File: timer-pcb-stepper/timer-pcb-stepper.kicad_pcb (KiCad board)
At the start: 4 copper layers, 75 x 69.5 mm, 27 parts, among them J1 JST_05, J10 JST_05, J2 JST_02, J3 JST_02, J4 JST_03, J5 JST_03, J6 JST_03, J7 JST_03, J8 JST_03_Led_panel, J9 JST_05, U2 ULN2003, U3 ULN2003, U4 ULN2003

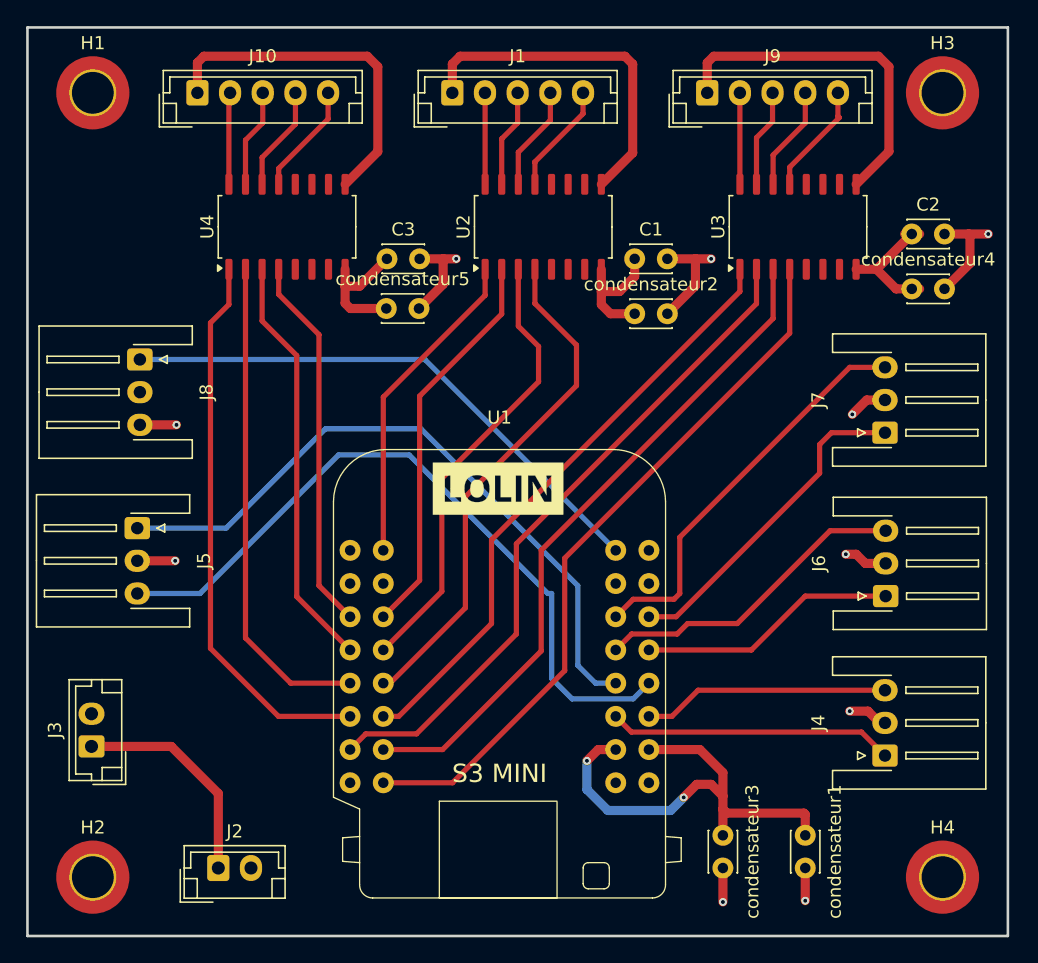
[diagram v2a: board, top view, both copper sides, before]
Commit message: rework des PCB stepper et led. création du PCB chargeur
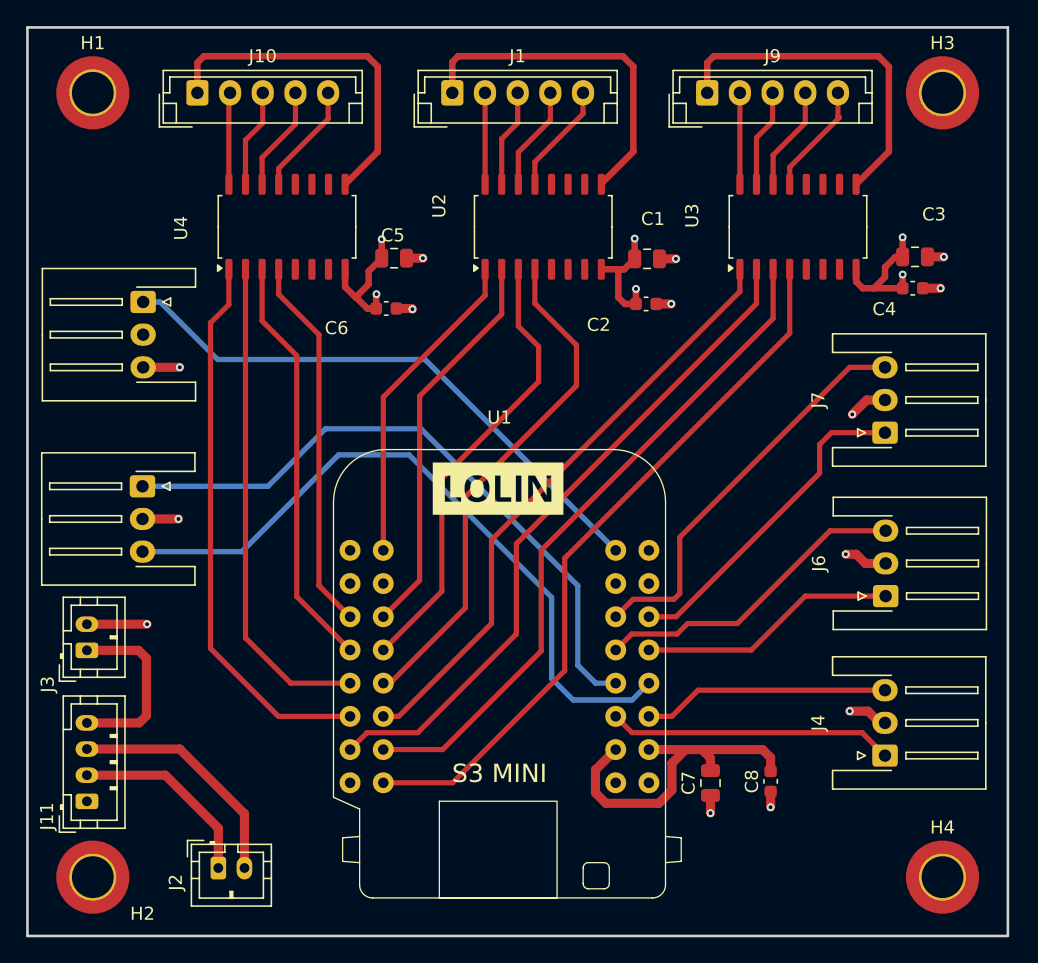
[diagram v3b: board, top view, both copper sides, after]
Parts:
- added J11: JST_04, Connector_JST:JST_PH_B4B-PH-K_1x04_P2.00mm_Vertical, F.Cu at (54.5, 99.2)
- C1: footprint Capacitor_THT:C_Disc_D3.0mm_W2.0mm_P2.50mm -> Capacitor_SMD:C_0805_2012Metric
- C2: renamed from condensateur2; footprint Capacitor_THT:C_Disc_D3.0mm_W2.0mm_P2.50mm -> Capacitor_SMD:C_0603_1608Metric
- C3: renamed from C2; footprint Capacitor_THT:C_Disc_D3.0mm_W2.0mm_P2.50mm -> Capacitor_SMD:C_0805_2012Metric
- C4: renamed from condensateur4; footprint Capacitor_THT:C_Disc_D3.0mm_W2.0mm_P2.50mm -> Capacitor_SMD:C_0603_1608Metric
- C5: renamed from C3; footprint Capacitor_THT:C_Disc_D3.0mm_W2.0mm_P2.50mm -> Capacitor_SMD:C_0805_2012Metric
- C6: renamed from condensateur5; footprint Capacitor_THT:C_Disc_D3.0mm_W2.0mm_P2.50mm -> Capacitor_SMD:C_0603_1608Metric
- C7: renamed from condensateur1; footprint Capacitor_THT:C_Disc_D3.0mm_W2.0mm_P2.50mm -> Capacitor_SMD:C_0805_2012Metric
- C8: renamed from condensateur3; footprint Capacitor_THT:C_Disc_D3.0mm_W2.0mm_P2.50mm -> Capacitor_SMD:C_0603_1608Metric
- J2: value JST_02 -> battery; footprint Connector_JST:JST_EH_B2B-EH-A_1x02_P2.50mm_Vertical -> Connector_JST:JST_PH_B2B-PH-K_1x02_P2.00mm_Vertical
- J3: value JST_02 -> On/off; footprint Connector_JST:JST_EH_B2B-EH-A_1x02_P2.50mm_Vertical -> Connector_JST:JST_PH_B2B-PH-K_1x02_P2.00mm_Vertical
- moved C7 8.28 mm to (102.2, 97.8), turned to 90 degrees
- moved J3 7.36 mm to (54.5, 87.7)
- moved C8 5.51 mm to (106.8, 97.7), turned to 90 degrees
- moved J8 4.41 mm to (58.9, 61.0)
- moved J5 3.22 mm to (58.8, 75.1)
- moved C3 1.77 mm to (117.9, 57.5)
- moved C2 1.15 mm to (97.3, 61.1)
- moved C1 0.95 mm to (97.4, 57.7)
- moved C5 0.55 mm to (78.0, 57.6)
- moved C4 0.09 mm to (117.7, 60.0), turned to 180 degrees
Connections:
- C1 pad 1: Net-(U2-GND) -> GND
- C1 pad 2: GND -> +5V
- C2 pad 1: Net-(U2-GND) -> GND
- C2 pad 2: GND -> +5V
- C3 pad 1: Net-(U3-GND) -> GND
- C3 pad 2: GND -> +5V
- C4 pad 1: Net-(U3-GND) -> +5V
- C5 pad 1: Net-(U4-GND) -> GND
- C5 pad 2: GND -> +5V
- C6 pad 1: Net-(U4-GND) -> GND
- C6 pad 2: GND -> +5V
- C7 pad 1: Net-(U1-GND-Pad29) -> +5V
- C7 pad 2: +5V -> GND
- C8 pad 1: Net-(U1-GND-Pad29) -> +5V
- C8 pad 2: +5V -> GND
- J2 pad 1: On -> GND_chargeur_input
- J2 pad 2: GND -> 5V_chargeur_input
- J3 pad 1: On -> On/off
- J8 pad 2: VCC -> +5V
- U1 pad 15: Net-(BT1-+) -> +5V
- U1 pad 29: Net-(U1-GND-Pad29) -> GND
- U1 pad 30: Net-(U1-GND-Pad29) -> GND
- U2 pad 8: Net-(U2-GND) -> GND
- U3 pad 8: Net-(U3-GND) -> GND
- U4 pad 8: Net-(U4-GND) -> GND
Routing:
- net Net-(U1-GND-Pad29): track 36.3 -> 0.00 mm, vias 2 -> 0
- net GND: track 39.4 -> 72.5 mm, vias 8 -> 11
- net 5V_chargeur_input: track 0.00 -> 18.3 mm
- net On: track 16.9 -> 0.00 mm
- net GND_chargeur_input: track 0.00 -> 14.8 mm
- net +5V: track 80.1 -> 94.8 mm, vias 2 -> 9
- net On/off: track 0.00 -> 14.0 mm
- net Net-(U3-GND): track 11.0 -> 0.00 mm
- net Net-(U2-GND): track 9.92 -> 0.00 mm
- net Net-(U4-GND): track 9.78 -> 0.00 mm
- net Net-(BT1--): track 5.10 -> 0.00 mm
- net Switch_motor_1_Down: track 55.6 -> 53.7 mm
- net Switch_motor_1_Up: track 51.4 -> 49.7 mm
- net WS2812_Led: track 42.4 -> 44.0 mm

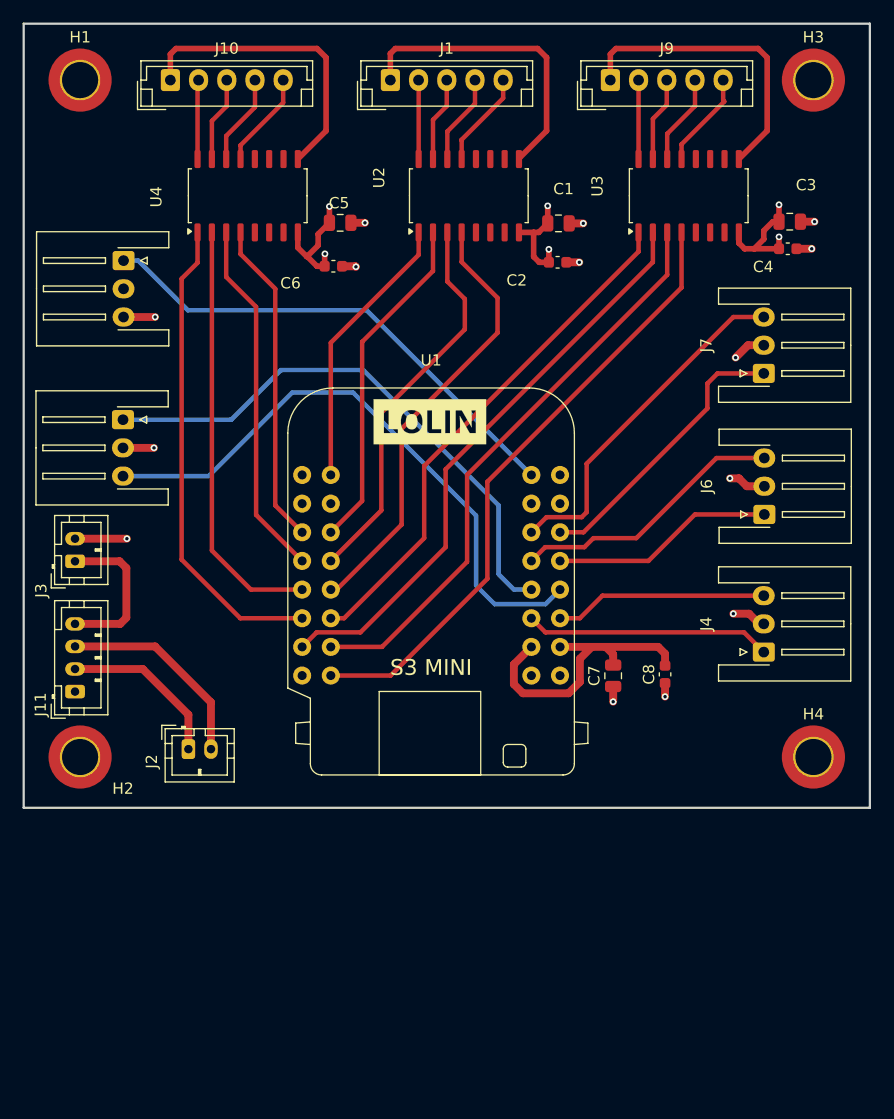
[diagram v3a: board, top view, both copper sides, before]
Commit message: suppression du dossier chargeur. integration de la partie chargeur usb-c sur le PCB stepper
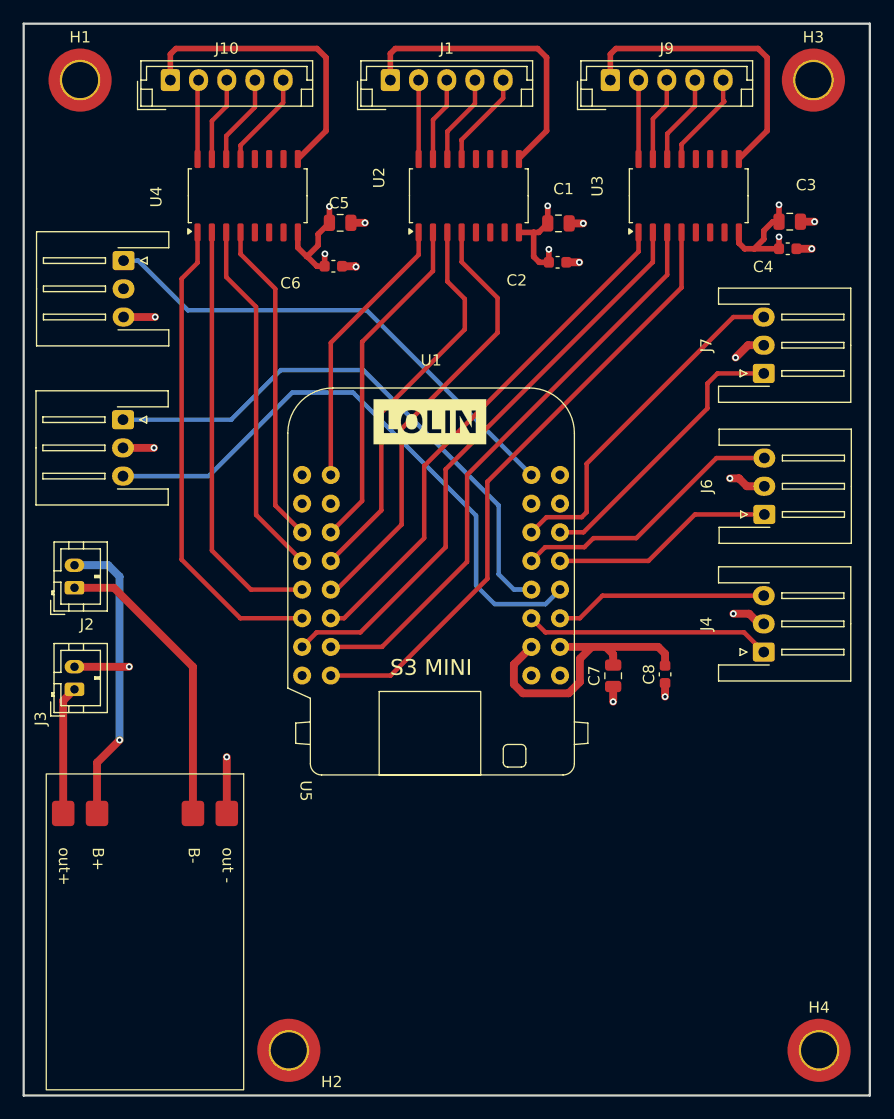
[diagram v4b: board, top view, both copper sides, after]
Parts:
- removed J11: JST_04, Connector_JST:JST_PH_B4B-PH-K_1x04_P2.00mm_Vertical
- added U5: ~, 1_My_Custom_Library:TP4056_chargeur_USB-C, F.Cu at (74.5, 106.5)
- moved H2 31.9 mm to (73.5, 131.0)
- moved H4 26.0 mm to (120.5, 131.0)
- moved J2 17.5 mm to (54.5, 90.0), turned to 90 degrees
- moved J3 11.4 mm to (54.5, 99.0)
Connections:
- J2 pad 1: GND_chargeur_input -> -BATT
- J2 pad 2: 5V_chargeur_input -> +BATT
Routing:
- net -BATT: track 0.00 -> 26.4 mm
- net +BATT: track 0.00 -> 26.2 mm, vias 0 -> 1
- net 5V_chargeur_input: track 18.3 -> 0.00 mm
- net GND_chargeur_input: track 14.8 -> 0.00 mm
- net GND: track 72.5 -> 77.5 mm, vias 11 -> 12
- net On/off: track 14.0 -> 11.4 mm
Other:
- board size 75 x 69.5 mm -> 75 x 95 mm

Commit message: reroutage des liaisons pour avoir un circuit imprimé plus propre.
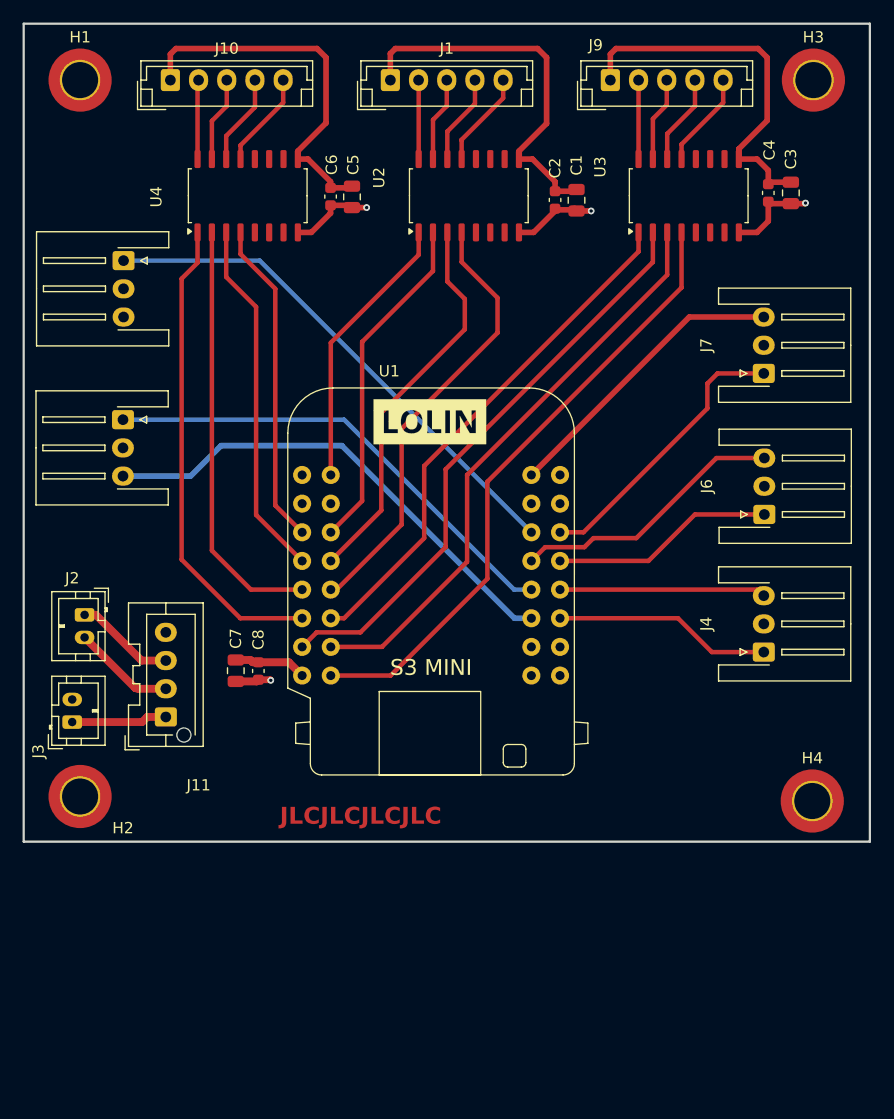
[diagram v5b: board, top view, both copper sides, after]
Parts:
- removed the G*** at (100.6, 59.8)
- removed U5: ~, 1_My_Custom_Library:TP4056_chargeur_USB-C
- added G***: LOGO, image.preety:QR_portfolio_10x10, B.Cu at (110.7, 103.3)
- added G***: LOGO, image.preety:QR_blog_electro_cafe_10x10, B.Cu at (88.0, 103.1)
- added J11: Conn_01x04_Pin, Connector_JST:JST_XA_B04B-XASK-1-A_1x04_P2.50mm_Vertical, F.Cu at (62.6, 101.5)
- added REF**: WEEE-Logo_5.6x8mm_SilkScreen, Symbol:WEEE-Logo_5.6x8mm_SilkScreen, B.Cu at (56.0, 53.6)
- moved C8 36.1 mm to (70.8, 97.4), turned to -90 degrees
- moved C7 33.5 mm to (68.8, 97.3), turned to -90 degrees
- moved H2 29.1 mm to (55.0, 108.5)
- moved H4 22.1 mm to (119.9, 108.9)
- moved C6 6.18 mm to (77.2, 55.3), turned to 90 degrees
- moved C2 5.53 mm to (97.1, 55.6), turned to 90 degrees
- moved C4 5.24 mm to (116.0, 55.0), turned to -90 degrees
- moved J3 2.91 mm to (54.3, 101.9)
- moved C1 2.60 mm to (99.0, 55.6), turned to 90 degrees
- moved J2 2.56 mm to (55.4, 92.4), turned to -90 degrees
- moved C3 2.55 mm to (118.0, 55.0), turned to 90 degrees
- moved C5 2.53 mm to (79.1, 55.4), turned to 90 degrees
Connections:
- U1 pad 17: WS2812_Led -> Switch_motor_3_Up
- U1 pad 21: Switch_motor_3_Up -> WS2812_Led
- U1 pad 26: Switch_motor_1_Down -> Switch_Led_control_Down
- U1 pad 27: Switch_Led_control_Up -> Switch_motor_1_Down
- U1 pad 28: Switch_Led_control_Down -> Switch_Led_control_Up
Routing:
- net GND: track 77.5 -> 26.7 mm, vias 12 -> 4
- net -BATT: track 26.4 -> 8.88 mm
- net +BATT: track 26.2 -> 9.08 mm, vias 1 -> 0
- net +5V: track 95.1 -> 106.0 mm, vias 9 -> 0
- net Switch_motor_1_Down: track 53.7 -> 43.7 mm
- net Switch_motor_1_Up: track 49.7 -> 42.4 mm
- net Switch_motor_3_Up: track 31.3 -> 26.6 mm
- net On/off: track 11.4 -> 8.49 mm
- net Switch_Led_control_Up: track 21.8 -> 19.3 mm
- net WS2812_Led: track 44.0 -> 46.1 mm
- net Switch_Led_control_Down: track 18.9 -> 18.3 mm
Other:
- board size 75 x 95 mm -> 75 x 72.5 mm
- board text added: "Blog electro café"
- board text added: "JLCJLCJLCJLC"
- board text added: "Portfolio"
- board text added: "Timer V1.0.0"
- board text added: "https://github.com/electro-cafe/ electro-cafe.github.io?tab=readme-ov-file"
